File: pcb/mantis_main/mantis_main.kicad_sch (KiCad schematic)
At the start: 113 parts, among them J1 Conn_01x02_Socket, J2 JST-PH, J3 Pin Header, J4 nice!nano extra, M1 SW_Mouse, M2 SW_Mouse, SW1 SW_SPDT, U1 74LVC1G17

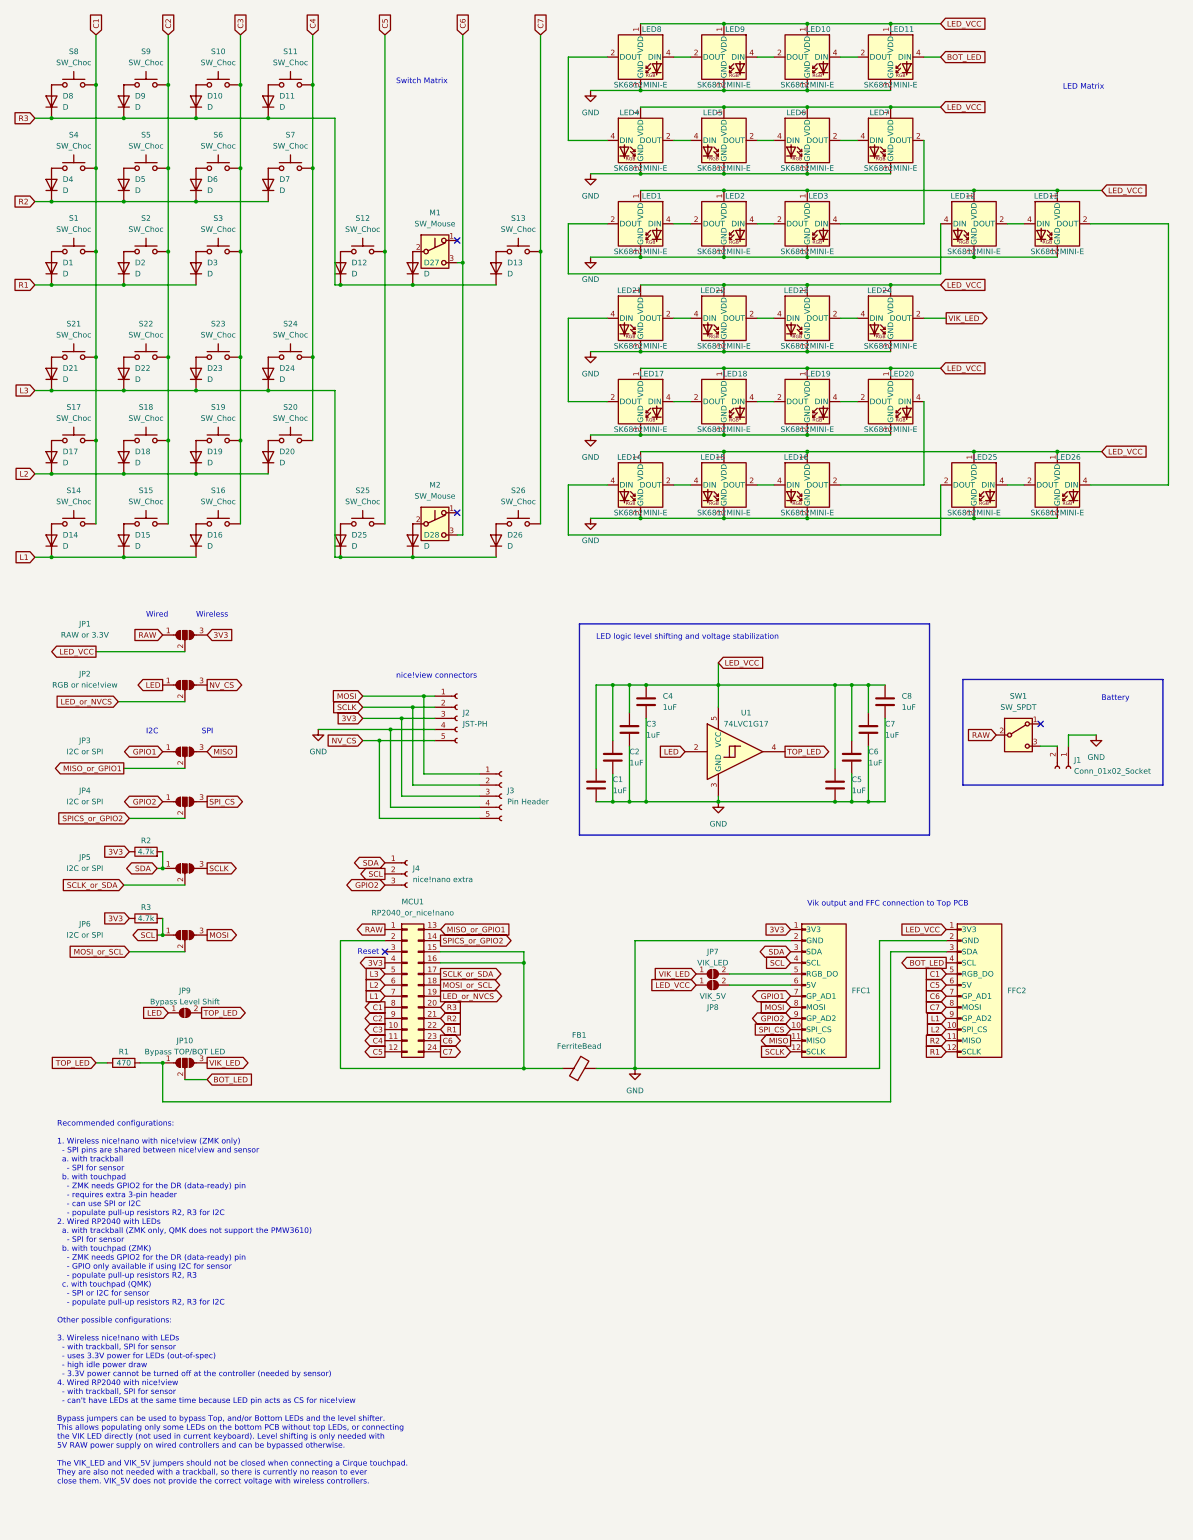
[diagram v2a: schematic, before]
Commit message: pcb: Update main and pmw3610 schematics
This should allow using PMW3610 and a nice!view display with the same SPI
pins on the controller:
- pmw3610: move MOTION (IRQ) signal to GPIO2 VIK wire
- pmw3610: move SDIO signal to MOSI VIK wire
- main: swap GPIO1/2 on the MCU so that GPIO2 is mapped to MISO
  Enables trackball without the extra 3-pin header

Update and reorgnanize configuration information.

Signed-off-by: Felix Kuehling <felix.kuehling@gmail.com>
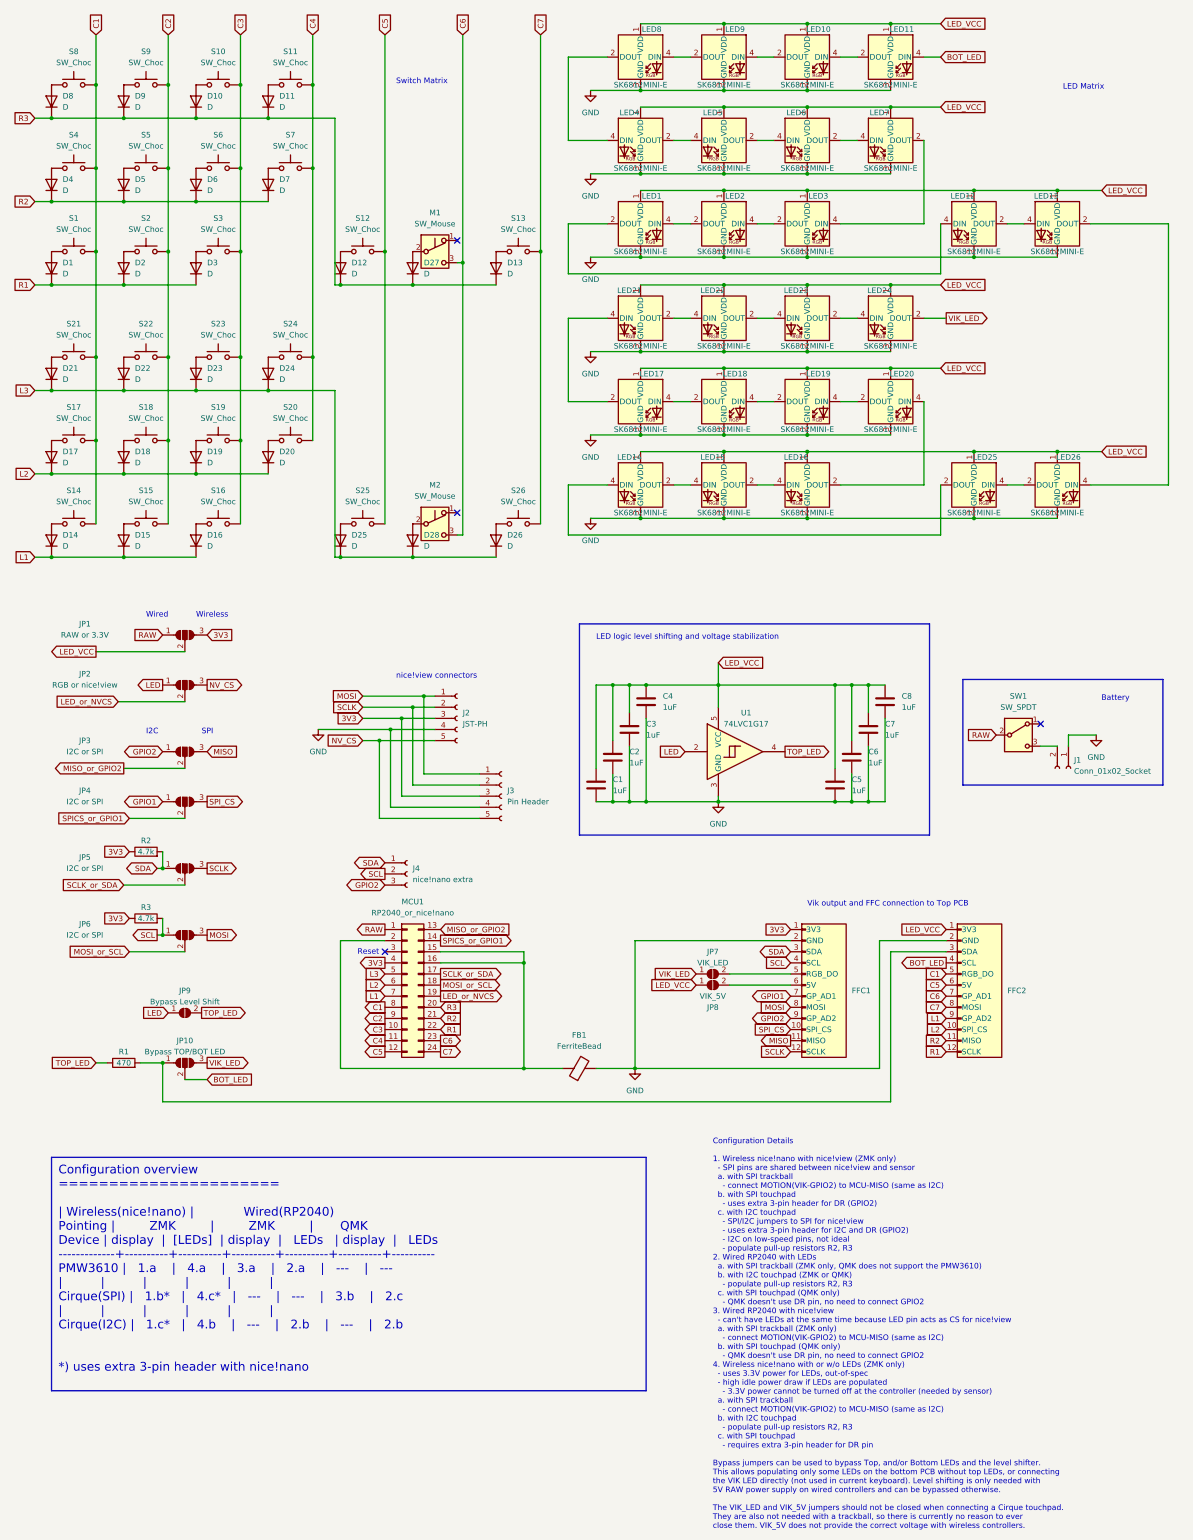
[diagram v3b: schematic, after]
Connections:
- net GPIO1: now also JP4.1 (A); no longer JP3.1 (A)
- net GPIO2: now also JP3.1 (A); no longer JP4.1 (A)
- net MISO_or_GPIO1 renamed MISO_or_GPIO2
- net SPICS_or_GPIO2 renamed SPICS_or_GPIO1
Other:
- note added: "Configuration Details 1. Wireless nice!nano with nice!view (ZMK only) - SPI pins are shared between nice!view and sensor a. with SPI trackball - connect MOTION(VIK-GPIO2) to MCU-MISO (same as I2C) b. with SPI touchpad - uses extra 3-pin header for DR (GPIO2) c. with I2C touchpad - SPI/I2C jumpers to SPI for nice!view - uses extra 3-pin header for I2C and DR (GPIO2) - I2C on low-speed pins, not id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"
- note removed: "Recommended configurations: 1. Wireless nice!nano with nice!view (ZMK only) - SPI pins are shared between nice!view and sensor a. with trackball - SPI for sensor b. with touchpad - ZMK needs GPIO2 for the DR (data-ready) pin - requires extra 3-pin header - can use SPI or I2C - populate pull-up resistors R2, R3 for I2C 2. Wired RP2040 with LEDs a. with trackball (ZMK only, QMK does not support the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"
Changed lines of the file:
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@@
     (fill (type none))
+  )
+  (text_box "Configuration overview\n======================\n\n             | Wireless(nice!nano) |             Wired(RP2040)\n    Pointing |         ZMK         |         ZMK         |       QMK\n      Device | display  |  [LEDs]  | display  |   LEDs   | display  |   LEDs\n-------------+----------+----------+----------+----------+----------+----------\n     PMW3610 |   1.a    |   4.a    |   3.a    |   2.a    |   ---    |   ---\n             |          |          |          |          |          |\n Cirque(SPI) |   1.b*   |   4.c*   |   ---    |   ---    |   3.b    |   2.c\n             |          |          |          |          |          |\n Cirque(I2C) |   1.c*   |   4.b    |   ---    |   2.b    |   ---    |   2.b\n\n\n*) uses extra 3-pin header with nice!nano"
+    (at 21.59 275.59 0) (size 135.89 53.34)
+    (stroke (width 0) (type default))
+    (fill (type none))
+    (effects (font (face "Courier 10 Pitch") (size 2 2)) (justify left top))
   )
   (text "Wired" (at 43.18 152.4 0)
@@
     (effects (font (size 1.27 1.27)) (justify left bottom))
   )
-  (text "Recommended configurations:\n\n1. Wireless nice!nano with nice!view (ZMK only)\n  - SPI pins are shared between nice!view and sensor\n  a. with trackball\n    - SPI for sensor\n  b. with touchpad\n    - ZMK needs GPIO2 for the DR (data-ready) pin\n    - requires extra 3-pin header\n    - can use SPI or I2C \n    - populate pull-up resistors R2, R3 for I2C\n2. Wired RP2040 with LEDs\n  a. with trackball (ZMK only, QMK does not support the PMW3610)\n    - SPI for sensor\n  b. with touchpad (ZMK)\n    - ZMK needs GPIO2 for the DR (data-ready) pin\n    - GPIO only available if using I2C for sensor\n    - populate pull-up resistors R2, R3\n  c. with touchpad (QMK)\n    - SPI or I2C for sensor\n    - populate pull-up resistors R2, R3 for I2C\n\nOther possible configurations:\n\n3. Wireless nice!nano with LEDs\n  - with trackball, SPI for sensor\n  - uses 3.3V power for LEDs (out-of-spec)\n  - high idle power draw\n  - 3.3V power cannot be turned off at the controller (needed by sensor)\n4. Wired RP2040 with nice!view\n  - with trackball, SPI for sensor\n  - can't have LEDs at the same time because LED pin acts as CS for nice!view\n\nBypass jumpers can be used to bypass Top, and/or Bottom LEDs and the level shifter.\nThis allows populating only some LEDs on the bottom PCB without top LEDs, or connecting\nthe VIK LED directly (not used in current keyboard). Level shifting is only needed with\n5V RAW power supply on wired controllers and can be bypassed otherwise.\n\nThe VIK_LED and VIK_5V jumpers should not be closed when connecting a Cirque touchpad.\nThey are also not needed with a trackball, so there is currently no reason to ever\nclose them. VIK_5V does not provide the correct voltage with wireless controllers."
-    (at 22.86 350.52 0)
+  (text "Configuration Details\n\n1. Wireless nice!nano with nice!view (ZMK only)\n  - SPI pins are shared between nice!view and sensor\n  a. with SPI trackball\n    - connect MOTION(VIK-GPIO2) to MCU-MISO (same as I2C)\n  b. with SPI touchpad\n    - uses extra 3-pin header for DR (GPIO2)\n  c. with I2C touchpad\n    - SPI/I2C jumpers to SPI for nice!view\n    - uses extra 3-pin header for I2C and DR (GPIO2)\n    - I2C on low-speed pins, not ideal\n    - populate pull-up resistors R2, R3\n2. Wired RP2040 with LEDs\n  a. with SPI trackball (ZMK only, QMK does not support the PMW3610)\n  b. with I2C touchpad (ZMK or QMK)\n    - populate pull-up resistors R2, R3\n  c. with SPI touchpad (QMK only)\n    - QMK doesn't use DR pin, no need to connect GPIO2\n3. Wired RP2040 with nice!view\n  - can't have LEDs at the same time because LED pin acts as CS for nice!view\n  a. with SPI trackball (ZMK only)\n    - connect MOTION(VIK-GPIO2) to MCU-MISO (same as I2C)\n  b. with SPI touchpad (QMK only)\n    - QMK doesn't use DR pin, no need to connect GPIO2\n4. Wireless nice!nano with or w/o LEDs (ZMK only)\n  - uses 3.3V power for LEDs, out-of-spec\n  - high idle power draw if LEDs are populated\n    - 3.3V power cannot be turned off at the controller (needed by sensor)\n  a. with SPI trackball\n    - connect MOTION(VIK-GPIO2) to MCU-MISO (same as I2C)\n  b. with I2C touchpad\n    - populate pull-up resistors R2, R3\n  c. with SPI touchpad\n    - requires extra 3-pin header for DR pin\n\nBypass jumpers can be used to bypass Top, and/or Bottom LEDs and the level shifter.\nThis allows populating only some LEDs on the bottom PCB without top LEDs, or connecting\nthe VIK LED directly (not used in current keyboard). Level shifting is only needed with\n5V RAW power supply on wired controllers and can be bypassed otherwise.\n\nThe VIK_LED and VIK_5V jumpers should not be closed when connecting a Cirque touchpad.\nThey are also not needed with a trackball, so there is currently no reason to ever\nclose them. VIK_5V does not provide the correct voltage with wireless controllers."
+    (at 172.72 360.68 0)
     (effects (font (size 1.27 1.27)) (justify left bottom))
   )
@@
     )
   )
-  (global_label "SPICS_or_GPIO2" (shape output) (at 110.49 226.06 0) (fields_autoplaced)
+  (global_label "SPICS_or_GPIO1" (shape output) (at 110.49 226.06 0) (fields_autoplaced)
     (effects (font (size 1.27 1.27)) (justify left))
     (property "Intersheetrefs" "${INTERSHEET_REFS}" (at 128.5942 226.06 0)
@@
     )
   )
-  (global_label "GPIO2" (shape bidirectional) (at 46.99 194.31 180) (fields_autoplaced)
+  (global_label "GPIO1" (shape bidirectional) (at 46.99 194.31 180) (fields_autoplaced)
     (effects (font (size 1.27 1.27)) (justify right))
     (property "Intersheetrefs" "${INTERSHEET_REFS}" (at 37.2087 194.31 0)
@@
     )
   )
-  (global_label "MISO_or_GPIO1" (shape input) (at 110.49 223.52 0) (fields_autoplaced)
+  (global_label "MISO_or_GPIO2" (shape input) (at 110.49 223.52 0) (fields_autoplaced)
     (effects (font (size 1.27 1.27)) (justify left))
     (property "Intersheetrefs" "${INTERSHEET_REFS}" (at 127.6266 223.52 0)
@@
     )
   )
-  (global_label "SPICS_or_GPIO2" (shape input) (at 39.37 198.12 180) (fields_autoplaced)
+  (global_label "SPICS_or_GPIO1" (shape input) (at 39.37 198.12 180) (fields_autoplaced)
     (effects (font (size 1.27 1.27)) (justify right))
     (property "Intersheetrefs" "${INTERSHEET_REFS}" (at 21.2658 198.12 0)
@@
     )
   )
-  (global_label "GPIO1" (shape bidirectional) (at 46.99 182.88 180) (fields_autoplaced)
+  (global_label "GPIO2" (shape bidirectional) (at 46.99 182.88 180) (fields_autoplaced)
     (effects (font (size 1.27 1.27)) (justify right))
     (property "Intersheetrefs" "${INTERSHEET_REFS}" (at 37.2087 182.88 0)
@@
     )
   )
-  (global_label "MISO_or_GPIO1" (shape output) (at 38.1 186.69 180) (fields_autoplaced)
+  (global_label "MISO_or_GPIO2" (shape output) (at 38.1 186.69 180) (fields_autoplaced)
     (effects (font (size 1.27 1.27)) (justify right))
     (property "Intersheetrefs" "${INTERSHEET_REFS}" (at 20.9634 186.69 0)

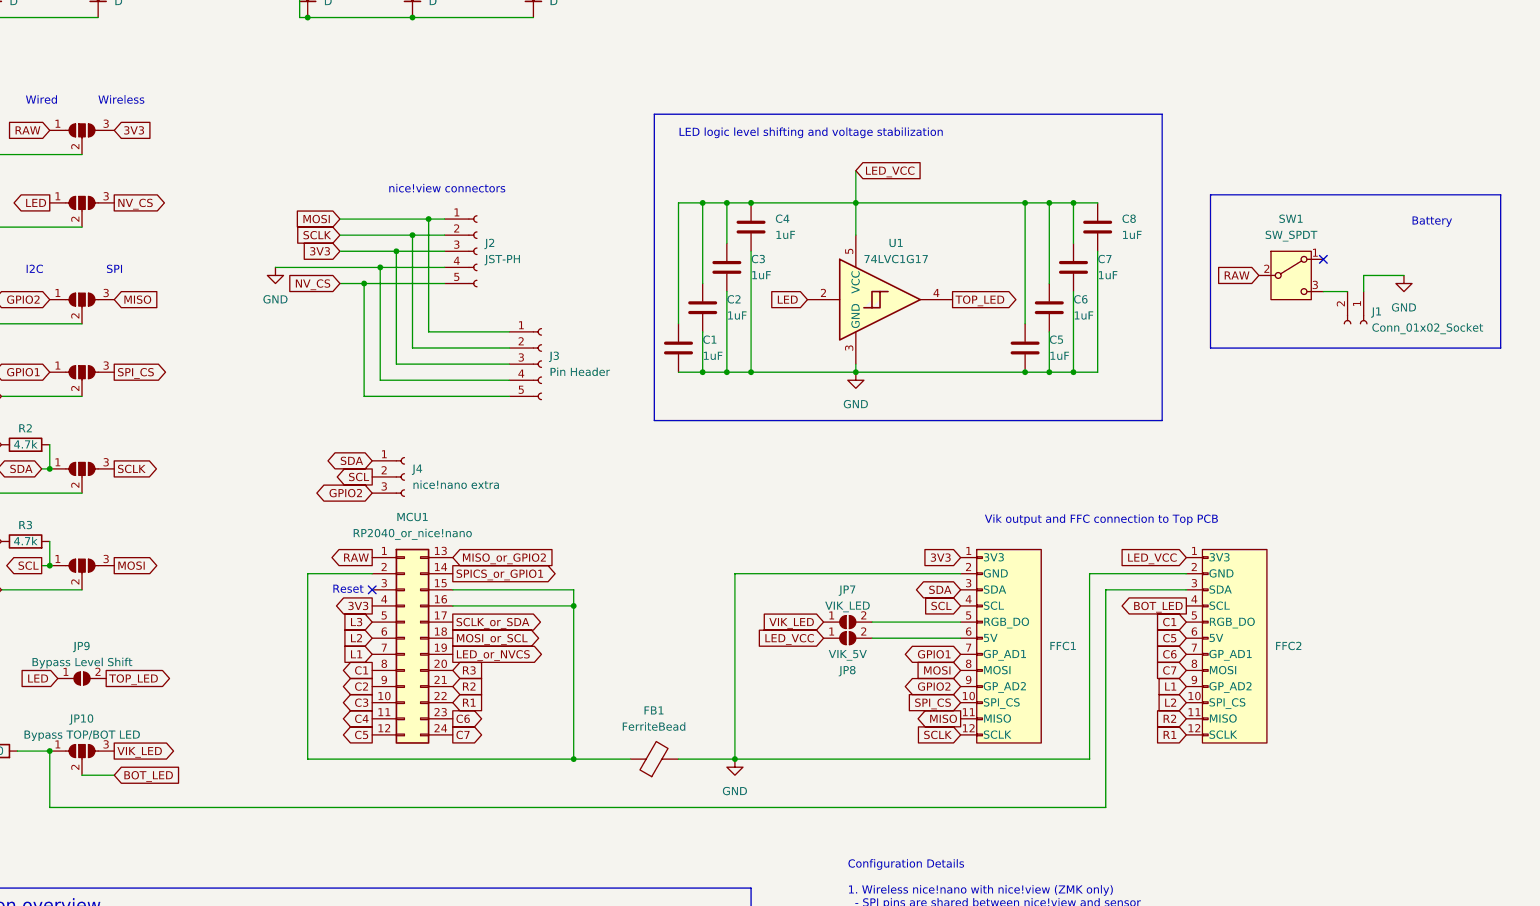
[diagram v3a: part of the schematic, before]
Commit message: pcb: Added reset switch
And random changes: renumbering some refs, GNDPWR symbol to create a
named net for it, changed jumper footprints

Signed-off-by: Felix Kuehling <felix.kuehling@gmail.com>
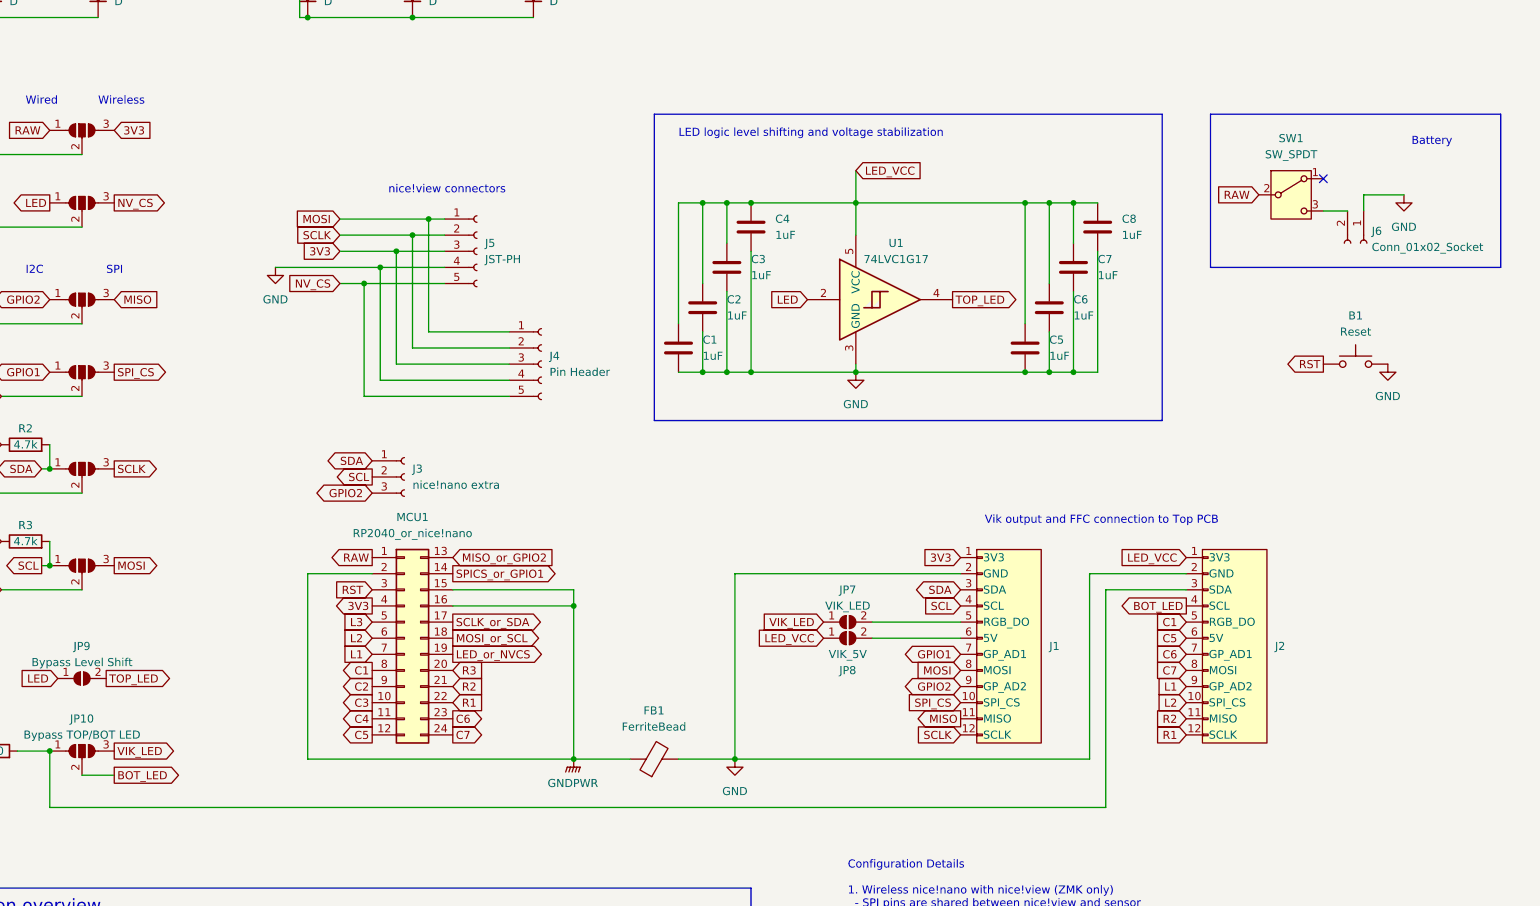
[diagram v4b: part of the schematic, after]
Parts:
- added B1: Reset, Button_Switch_SMD:SW_SPST_SKQG_WithoutStem, symbol Switch:SW_Push
- JP1, JP10, JP2, JP3, JP4, JP5, JP6: footprint Jumper:SolderJumper-3_P2.0mm_Open_TrianglePad1.0x1.5mm -> Jumper:SolderJumper-3_P1.3mm_Open_RoundedPad1.0x1.5mm
- JP7, JP8, JP9: footprint Jumper:SolderJumper-2_P1.3mm_Open_TrianglePad1.0x1.5mm -> Jumper:SolderJumper-2_P1.3mm_Open_RoundedPad1.0x1.5mm
- renumbered FFC1 to J1, FFC2 to J2, J4 to J3, J3 to J4, J2 to J5, J1 to J6
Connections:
- net GND: now also B1.2
- net GNDPWR: now reaches FB1.1, MCU1.15 (Pin_15), MCU1.16 (Pin_16), MCU1.2 (Pin_2)
- net RST: now reaches MCU1.3 (Pin_3)
- net RST: now also B1.1
- no-connect marks 4 -> 3
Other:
- note removed: "Reset"
- moved on the sheet: J6, SW1
